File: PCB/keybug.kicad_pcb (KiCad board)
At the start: 2 copper layers, 21 x 96.5 mm, 8 parts, among them U2 rp2040-zero

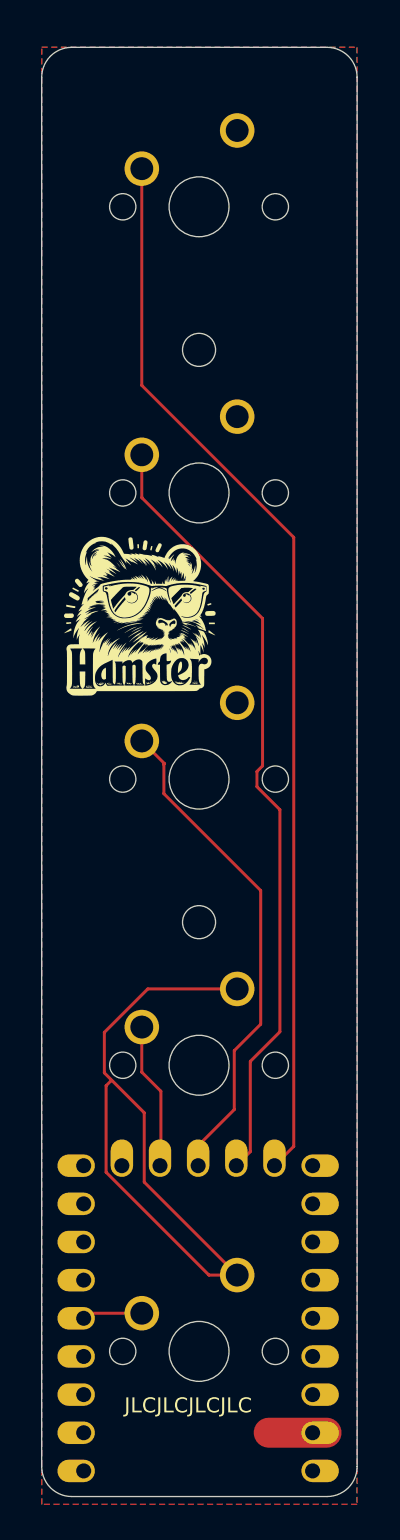
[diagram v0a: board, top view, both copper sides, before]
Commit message: PCB+Firmware: make board reversible
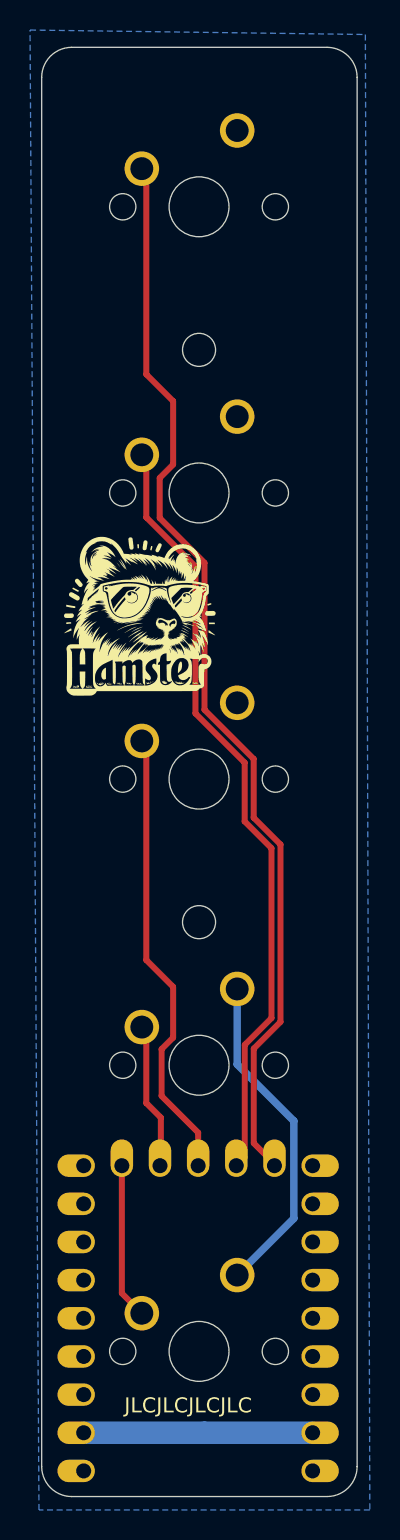
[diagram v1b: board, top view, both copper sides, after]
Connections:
- U2 pad 10: unconnected-(U2-9-Pad10) -> SW5
- U2 pad 2: unconnected-(U2-1-Pad2) -> GND
- U2 pad 23: +5V -> unconnected-(U2-5V-Pad23)
- U2 pad 5: SW5 -> unconnected-(U2-4-Pad5)
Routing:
- net GND: track 52.1 -> 38.0 mm
- net SW5: track 4.01 -> 10.4 mm
- net SW3: track 33.2 -> 31.8 mm
- net SW1: track 71.0 -> 72.2 mm
- net SW2: track 52.6 -> 51.8 mm
- removed copper zone on F.Cu, net GND

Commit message: Add LEDs to PCB
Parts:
- added LED1: MX_SK6812MINI-E, PCM_marbastlib-mx:LED_MX_6028R-ROT, F.Cu at (91.9, 43.6)
- added LED2: MX_SK6812MINI-E, PCM_marbastlib-mx:LED_MX_6028R-ROT, F.Cu at (91.9, 62.7)
- added LED3: MX_SK6812MINI-E, PCM_marbastlib-mx:LED_MX_6028R-ROT, F.Cu at (91.9, 81.7)
- added LED4: MX_SK6812MINI-E, PCM_marbastlib-mx:LED_MX_6028R-ROT, F.Cu at (91.9, 100.8)
- added LED5: MX_SK6812MINI-E, PCM_marbastlib-mx:LED_MX_6028R-ROT, F.Cu at (91.9, 119.8)
- turned MX1 to -90 degrees
- turned MX2 to -90 degrees
- turned MX3 to -90 degrees
- turned MX4 to -90 degrees
- turned MX5 to -90 degrees
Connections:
- U2 pad 1: unconnected-(U2-0-Pad1) -> VDD
- U2 pad 15: unconnected-(U2-14-Pad15) -> RGB
- U2 pad 23: unconnected-(U2-5V-Pad23) -> VDD
- U2 pad 9: unconnected-(U2-8-Pad9) -> RGB
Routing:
- net VDD: track 0.00 -> 126.5 mm
- net RGB: track 0.00 -> 38.4 mm, vias 0 -> 1
- net GND: track 38.0 -> 54.8 mm, vias 0 -> 5
- net Net-(LED4-DIN): track 0.00 -> 14.9 mm
- net Net-(LED1-DIN): track 0.00 -> 14.5 mm
- net Net-(LED2-DIN): track 0.00 -> 14.2 mm
- net Net-(LED3-DIN): track 0.00 -> 14.2 mm
- net SW4: track 9.69 -> 14.1 mm
- net SW1: track 72.2 -> 70.3 mm
- net SW5: track 10.4 -> 11.7 mm
